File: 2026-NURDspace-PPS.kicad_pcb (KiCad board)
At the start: 4 copper layers, 50 x 50 mm, 4 parts

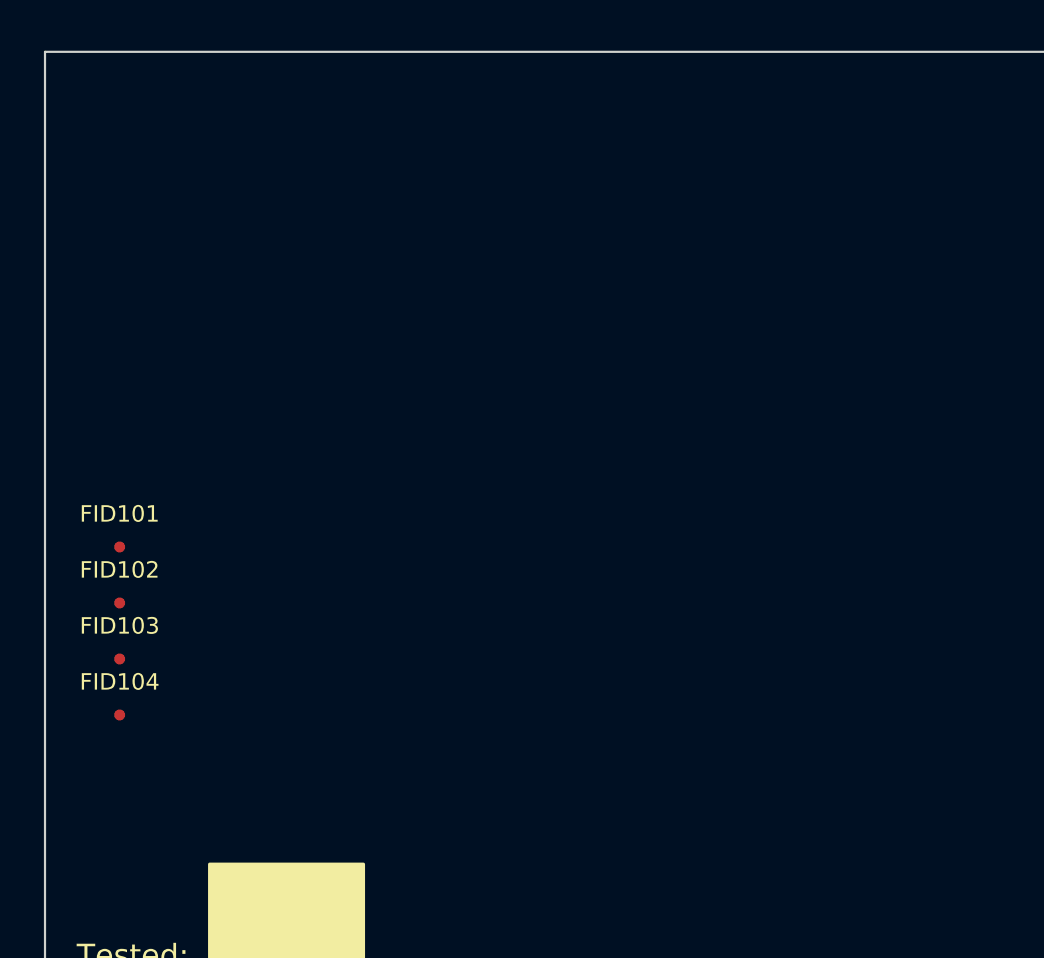
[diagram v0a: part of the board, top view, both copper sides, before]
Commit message: Started on gathering parts
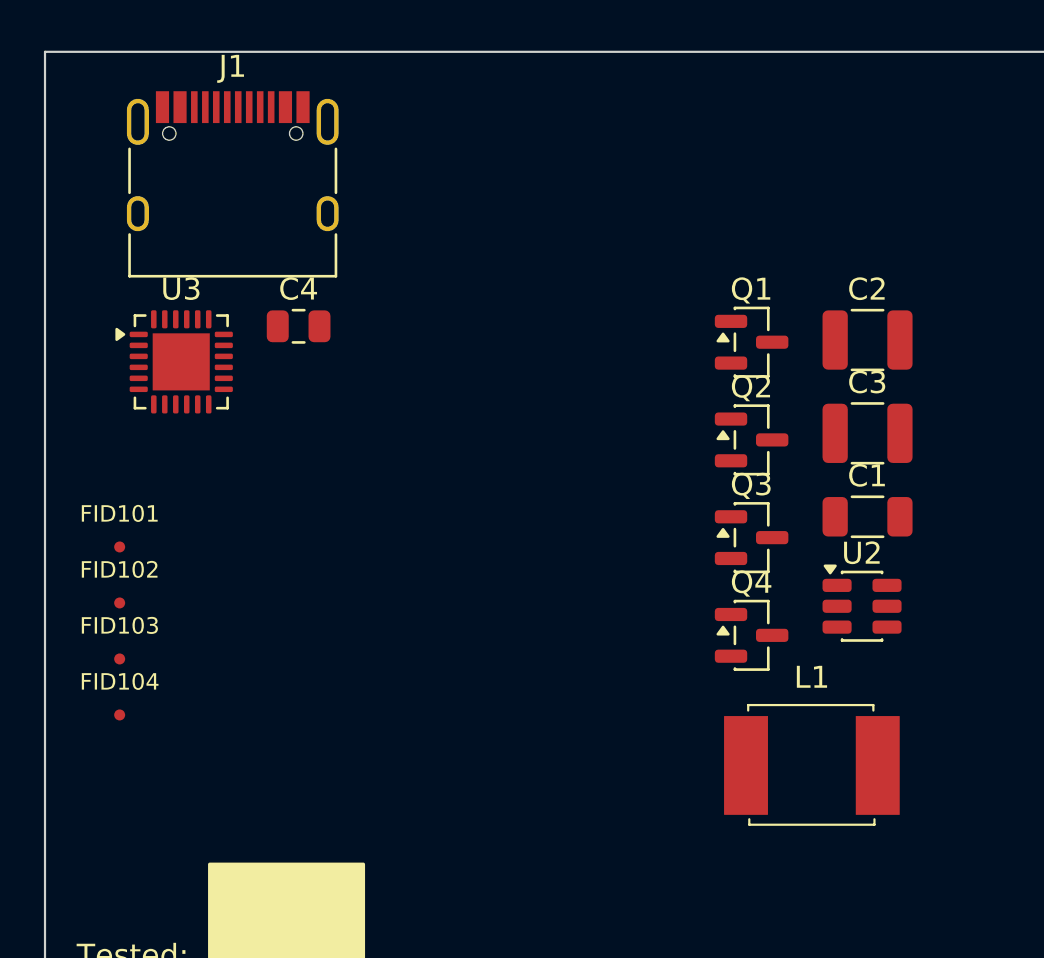
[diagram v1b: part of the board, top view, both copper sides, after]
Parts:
- added C1: 6.8uF, Capacitor_SMD:C_1206_3216Metric, F.Cu at (137.5, 71.2)
- added C2: 47uF, Capacitor_SMD:C_1210_3225Metric, F.Cu at (137.5, 63.1)
- added C3: 47uF, Capacitor_SMD:C_1210_3225Metric, F.Cu at (137.5, 67.4)
- added C4: 100nF, Capacitor_SMD:C_0805_2012Metric, F.Cu at (111.5, 62.5)
- added J1: UJ20-C-H-C-4-SMT-TR, 0_NRD_footprints:USB_C_Receptacle_SSKY_UJ20-C-H-C-4-SMT-TR, F.Cu at (108.5, 56.3)
- added L1: 4.7uH, 0_NRD_footprints:FB_2020_5650Metric, F.Cu at (134.9, 82.5)
- added Q1: BSN20, Package_TO_SOT_SMD:SOT-23, F.Cu at (132.2, 63.2)
- added Q2: BSN20, Package_TO_SOT_SMD:SOT-23, F.Cu at (132.2, 67.7)
- added Q3: BSN20, Package_TO_SOT_SMD:SOT-23, F.Cu at (132.2, 72.1)
- added Q4: BSN20, Package_TO_SOT_SMD:SOT-23, F.Cu at (132.2, 76.6)
- added U2: 3.3V, Package_TO_SOT_SMD:TSOT-23-6, F.Cu at (137.2, 75.2)
- added U3: AP33772S, Package_DFN_QFN:QFN-24-1EP_4x4mm_P0.5mm_EP2.6x2.6mm, F.Cu at (106.2, 64.1)

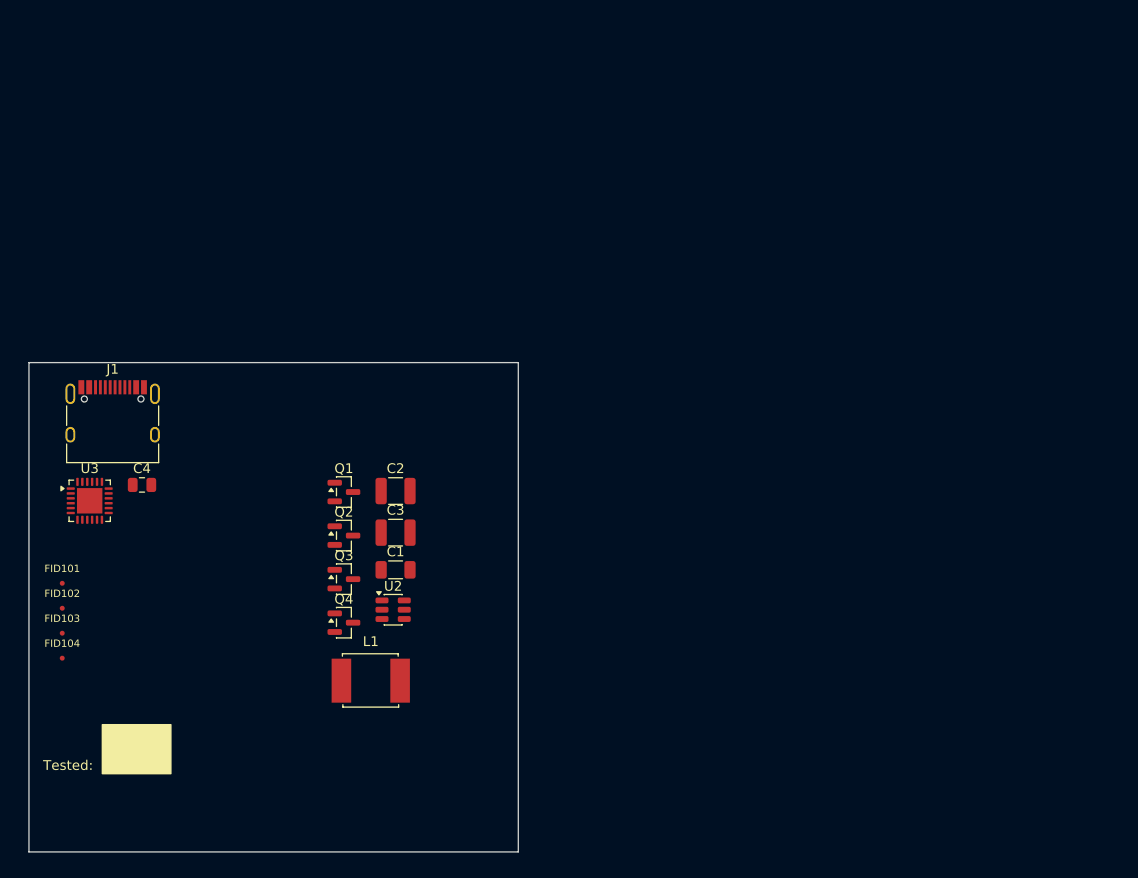
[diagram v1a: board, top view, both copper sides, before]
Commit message: Added all components
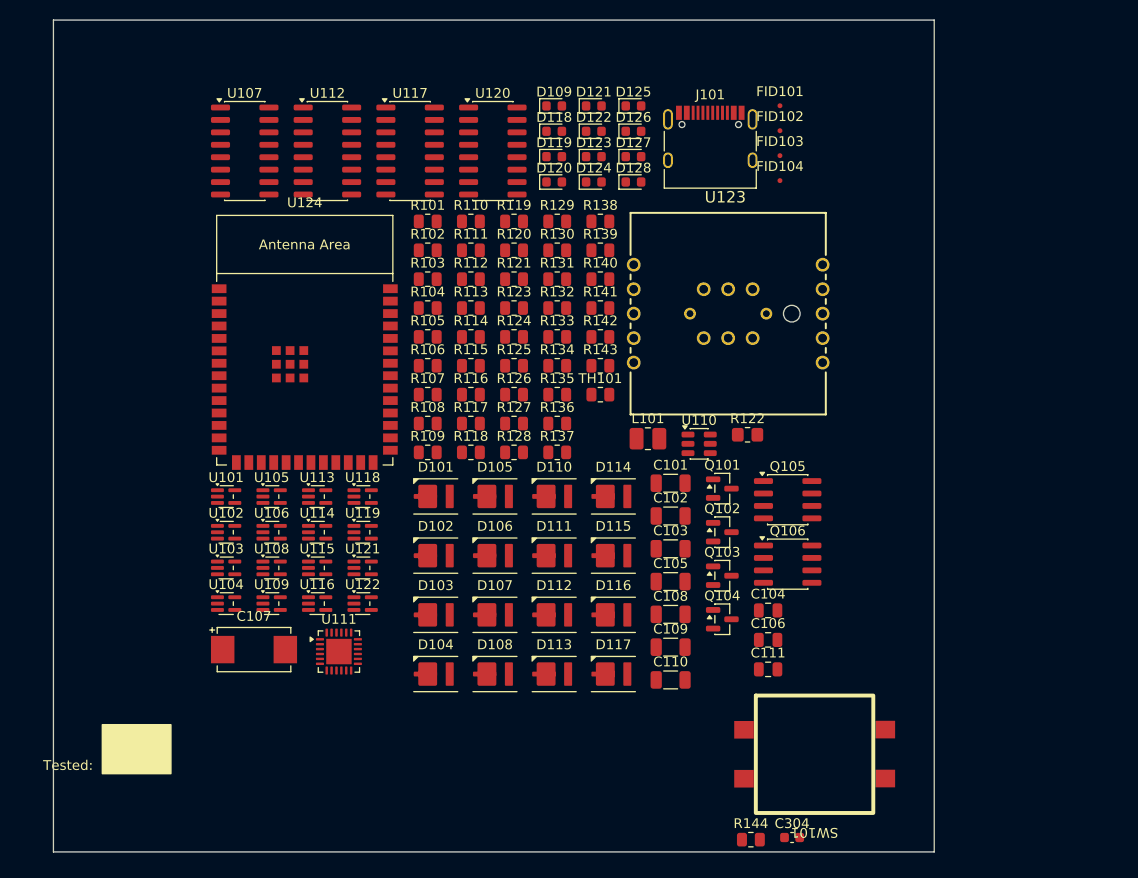
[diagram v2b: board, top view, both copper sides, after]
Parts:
- removed C1: 6.8uF, Capacitor_SMD:C_1206_3216Metric
- removed C2, C3: 47uF, Capacitor_SMD:C_1210_3225Metric
- removed C4: 100nF, Capacitor_SMD:C_0805_2012Metric
- removed J1: UJ20-C-H-C-4-SMT-TR, 0_NRD_footprints:USB_C_Receptacle_SSKY_UJ20-C-H-C-4-SMT-TR
- removed L1: 4.7uH, 0_NRD_footprints:FB_2020_5650Metric
- removed Q1, Q2, Q3, Q4: BSN20, Package_TO_SOT_SMD:SOT-23
- removed U2: 3.3V, Package_TO_SOT_SMD:TSOT-23-6
- removed U3: AP33772S, Package_DFN_QFN:QFN-24-1EP_4x4mm_P0.5mm_EP2.6x2.6mm
- added C101: 6.8uF, Capacitor_SMD:C_1206_3216Metric, F.Cu at (165.6, 62.3)
- added C102: 6.8uF, Capacitor_SMD:C_1206_3216Metric, F.Cu at (165.6, 65.7)
- added C103: 6.8uF, Capacitor_SMD:C_1206_3216Metric, F.Cu at (165.6, 69.0)
- added C104: 100nF, Capacitor_SMD:C_0805_2012Metric, F.Cu at (175.5, 75.3)
- added C105: 1uF, Capacitor_SMD:C_1206_3216Metric, F.Cu at (165.6, 72.4)
- added C106: 100nF, Capacitor_SMD:C_0805_2012Metric, F.Cu at (175.5, 78.3)
- added C107: 180uF, 0_NRD_footprints:CP_Wurth_WCAP-PHLE-L7.3W4.3H1.9, F.Cu at (123.0, 79.3)
- added C108: 6.8uF, Capacitor_SMD:C_1206_3216Metric, F.Cu at (165.6, 75.7)
- added C109: 1uF, Capacitor_SMD:C_1206_3216Metric, F.Cu at (165.6, 79.1)
- added C110: 6.8uF, Capacitor_SMD:C_1206_3216Metric, F.Cu at (165.6, 82.4)
- added C111: 100nF, Capacitor_SMD:C_0805_2012Metric, F.Cu at (175.5, 81.3)
- added C304: 100nF, Capacitor_SMD:C_0603_1608Metric, F.Cu at (178.0, 98.5)
- added D101: MXA8-PW40-0000, 0_NRD_footprints:LED_Luxeon3535_3.5x3.7mm, F.Cu at (141.6, 63.7)
- added D102: MXA8-PW40-0000, 0_NRD_footprints:LED_Luxeon3535_3.5x3.7mm, F.Cu at (141.6, 69.7)
- added D103: MXA8-PW40-0000, 0_NRD_footprints:LED_Luxeon3535_3.5x3.7mm, F.Cu at (141.6, 75.8)
- added D104: MXA8-PW40-0000, 0_NRD_footprints:LED_Luxeon3535_3.5x3.7mm, F.Cu at (141.6, 81.8)
- added D105: MXA8-PW40-0000, 0_NRD_footprints:LED_Luxeon3535_3.5x3.7mm, F.Cu at (147.6, 63.7)
- added D106: MXA8-PW40-0000, 0_NRD_footprints:LED_Luxeon3535_3.5x3.7mm, F.Cu at (147.6, 69.7)
- added D107: MXA8-PW40-0000, 0_NRD_footprints:LED_Luxeon3535_3.5x3.7mm, F.Cu at (147.6, 75.8)
- added D108: MXA8-PW40-0000, 0_NRD_footprints:LED_Luxeon3535_3.5x3.7mm, F.Cu at (147.6, 81.8)
- added D109: amber, LED_SMD:LED_0603_1608Metric, F.Cu at (153.7, 23.8)
- added D110: MXA8-PW40-0000, 0_NRD_footprints:LED_Luxeon3535_3.5x3.7mm, F.Cu at (153.7, 63.7)
- added D111: MXA8-PW40-0000, 0_NRD_footprints:LED_Luxeon3535_3.5x3.7mm, F.Cu at (153.7, 69.7)
- added D112: MXA8-PW40-0000, 0_NRD_footprints:LED_Luxeon3535_3.5x3.7mm, F.Cu at (153.7, 75.8)
- added D113: MXA8-PW40-0000, 0_NRD_footprints:LED_Luxeon3535_3.5x3.7mm, F.Cu at (153.7, 81.8)
- added D114: MXA8-PW40-0000, 0_NRD_footprints:LED_Luxeon3535_3.5x3.7mm, F.Cu at (159.7, 63.7)
- added D115: MXA8-PW40-0000, 0_NRD_footprints:LED_Luxeon3535_3.5x3.7mm, F.Cu at (159.7, 69.7)
- added D116: MXA8-PW40-0000, 0_NRD_footprints:LED_Luxeon3535_3.5x3.7mm, F.Cu at (159.7, 75.8)
- added D117: MXA8-PW40-0000, 0_NRD_footprints:LED_Luxeon3535_3.5x3.7mm, F.Cu at (159.7, 81.8)
- added D118: brightgreen, LED_SMD:LED_0603_1608Metric, F.Cu at (153.7, 26.4)
- added D119: Led_0603_superred_generic, LED_SMD:LED_0603_1608Metric, F.Cu at (153.7, 29.0)
- added D120: Led_0603_superred_generic, LED_SMD:LED_0603_1608Metric, F.Cu at (153.7, 31.5)
- added D121: Led_0603_superred_generic, LED_SMD:LED_0603_1608Metric, F.Cu at (157.7, 23.8)
- added D122: Led_0603_superred_generic, LED_SMD:LED_0603_1608Metric, F.Cu at (157.7, 26.4)
- added D123: Led_0603_superred_generic, LED_SMD:LED_0603_1608Metric, F.Cu at (157.7, 29.0)
- added D124: Led_0603_superred_generic, LED_SMD:LED_0603_1608Metric, F.Cu at (157.7, 31.5)
- added D125: Led_0603_superred_generic, LED_SMD:LED_0603_1608Metric, F.Cu at (161.8, 23.8)
- added D126: Led_0603_superred_generic, LED_SMD:LED_0603_1608Metric, F.Cu at (161.8, 26.4)
- added D127: Led_0603_superred_generic, LED_SMD:LED_0603_1608Metric, F.Cu at (161.8, 29.0)
- added D128: Led_0603_superred_generic, LED_SMD:LED_0603_1608Metric, F.Cu at (161.8, 31.5)
- added J101: UJ20-C-H-C-4-SMT-TR, 0_NRD_footprints:USB_C_Receptacle_SSKY_UJ20-C-H-C-4-SMT-TR, F.Cu at (169.6, 28.3)
- added L101: 4.7uH, Inductor_SMD:L_1008_2520Metric_Pad1.43x2.20mm_HandSolder, F.Cu at (163.2, 57.8)
- added Q101: BSN20, Package_TO_SOT_SMD:SOT-23, F.Cu at (170.8, 62.9)
- added Q102: BSN20, Package_TO_SOT_SMD:SOT-23, F.Cu at (170.8, 67.3)
- added Q103: BSN20, Package_TO_SOT_SMD:SOT-23, F.Cu at (170.8, 71.8)
- added Q104: BSN20, Package_TO_SOT_SMD:SOT-23, F.Cu at (170.8, 76.2)
- added Q105: XTR_NFET_SI4134, Package_SO:SOIC-8_3.9x4.9mm_P1.27mm, F.Cu at (177.5, 64.0)
- added Q106: XTR_NFET_SI4134, Package_SO:SOIC-8_3.9x4.9mm_P1.27mm, F.Cu at (177.5, 70.6)
- added R101: 5K1, Resistor_SMD:R_0805_2012Metric, F.Cu at (140.7, 35.6)
- added R102: 5K1, Resistor_SMD:R_0805_2012Metric, F.Cu at (140.7, 38.5)
- added R103: 5K1, Resistor_SMD:R_0805_2012Metric, F.Cu at (140.7, 41.5)
- added R104: 5K1, Resistor_SMD:R_0805_2012Metric, F.Cu at (140.7, 44.4)
- added R105: 39R, Resistor_SMD:R_0805_2012Metric, F.Cu at (140.7, 47.4)
- added R106: 39R, Resistor_SMD:R_0805_2012Metric, F.Cu at (140.7, 50.3)
- added R107: 39R, Resistor_SMD:R_0805_2012Metric, F.Cu at (140.7, 53.3)
- added R108: 39R, Resistor_SMD:R_0805_2012Metric, F.Cu at (140.7, 56.2)
- added R109: 39R, Resistor_SMD:R_0805_2012Metric, F.Cu at (140.7, 59.2)
- added R110: 39R, Resistor_SMD:R_0805_2012Metric, F.Cu at (145.2, 35.6)
- added R111: 39R, Resistor_SMD:R_0805_2012Metric, F.Cu at (145.2, 38.5)
- added R112: 39R, Resistor_SMD:R_0805_2012Metric, F.Cu at (145.2, 41.5)
- added R113: 5K1, Resistor_SMD:R_0805_2012Metric, F.Cu at (145.2, 44.4)
- added R114: 5K1, Resistor_SMD:R_0805_2012Metric, F.Cu at (145.2, 47.4)
- added R115: 5K1, Resistor_SMD:R_0805_2012Metric, F.Cu at (145.2, 50.3)
- added R116: 5K1, Resistor_SMD:R_0805_2012Metric, F.Cu at (145.2, 53.3)
- added R117: 39R, Resistor_SMD:R_0805_2012Metric, F.Cu at (145.2, 56.2)
- added R118: 39R, Resistor_SMD:R_0805_2012Metric, F.Cu at (145.2, 59.2)
- added R119: 39R, Resistor_SMD:R_0805_2012Metric, F.Cu at (149.6, 35.6)
- added R120: 39R, Resistor_SMD:R_0805_2012Metric, F.Cu at (149.6, 38.5)
- added R121: 5K1, Resistor_SMD:R_0805_2012Metric, F.Cu at (149.6, 41.5)
- added R122: 5mR, Resistor_SMD:R_0805_2012Metric_Pad1.20x1.40mm_HandSolder, F.Cu at (173.4, 57.4)
- added R123: 39R, Resistor_SMD:R_0805_2012Metric, F.Cu at (149.6, 44.4)
- added R124: 39R, Resistor_SMD:R_0805_2012Metric, F.Cu at (149.6, 47.4)
- added R125: 39R, Resistor_SMD:R_0805_2012Metric, F.Cu at (149.6, 50.3)
- added R126: 39R, Resistor_SMD:R_0805_2012Metric, F.Cu at (149.6, 53.3)
- added R127: 5K1, Resistor_SMD:R_0805_2012Metric, F.Cu at (149.6, 56.2)
- added R128: 5K1, Resistor_SMD:R_0805_2012Metric, F.Cu at (149.6, 59.2)
- added R129: 180R, Resistor_SMD:R_0805_2012Metric, F.Cu at (154.0, 35.6)
- added R130: 5K1, Resistor_SMD:R_0805_2012Metric, F.Cu at (154.0, 38.5)
- added R131: 5K1, Resistor_SMD:R_0805_2012Metric, F.Cu at (154.0, 41.5)
- added R132: 270R, Resistor_SMD:R_0805_2012Metric, F.Cu at (154.0, 44.4)
- added R133: 270R, Resistor_SMD:R_0805_2012Metric, F.Cu at (154.0, 47.4)
- added R134: 270R, Resistor_SMD:R_0805_2012Metric, F.Cu at (154.0, 50.3)
- added R135: 270R, Resistor_SMD:R_0805_2012Metric, F.Cu at (154.0, 53.3)
- added R136: 270R, Resistor_SMD:R_0805_2012Metric, F.Cu at (154.0, 56.2)
- added R137: 5K1, Resistor_SMD:R_0805_2012Metric, F.Cu at (154.0, 59.2)
- added R138: 5K1, Resistor_SMD:R_0805_2012Metric, F.Cu at (158.4, 35.6)
- added R139: 270R, Resistor_SMD:R_0805_2012Metric, F.Cu at (158.4, 38.5)
- added R140: 270R, Resistor_SMD:R_0805_2012Metric, F.Cu at (158.4, 41.5)
- added R141: 270R, Resistor_SMD:R_0805_2012Metric, F.Cu at (158.4, 44.4)
- added R142: 270R, Resistor_SMD:R_0805_2012Metric, F.Cu at (158.4, 47.4)
- added R143: 270R, Resistor_SMD:R_0805_2012Metric, F.Cu at (158.4, 50.3)
- added R144: 5K1, Resistor_SMD:R_0805_2012Metric, F.Cu at (173.8, 98.7)
- added SW101: 430172085816, 0_NRD_footprints:btn_momentary_430172085816, F.Cu at (180.3, 90.0)
- added TH101: NTCS0805, Resistor_SMD:R_0805_2012Metric, F.Cu at (158.4, 53.3)
- added U101: 1G126, Package_TO_SOT_SMD:SOT-353_SC-70-5, F.Cu at (120.1, 63.7)
- added U102: 1G126, Package_TO_SOT_SMD:SOT-353_SC-70-5, F.Cu at (120.1, 67.3)
- added U103: 1G126, Package_TO_SOT_SMD:SOT-353_SC-70-5, F.Cu at (120.1, 71.0)
- added U104: 1G126, Package_TO_SOT_SMD:SOT-353_SC-70-5, F.Cu at (120.1, 74.6)
- added U105: 1G126, Package_TO_SOT_SMD:SOT-353_SC-70-5, F.Cu at (124.8, 63.7)
- added U106: 1G126, Package_TO_SOT_SMD:SOT-353_SC-70-5, F.Cu at (124.8, 67.3)
- added U107: 74HC595, Package_SO:SOIC-16_3.9x9.9mm_P1.27mm, F.Cu at (122.0, 28.4)
- added U108: 1G126, Package_TO_SOT_SMD:SOT-353_SC-70-5, F.Cu at (124.8, 71.0)
- added U109: 1G126, Package_TO_SOT_SMD:SOT-353_SC-70-5, F.Cu at (124.8, 74.6)
- added U110: 3.3V, Package_TO_SOT_SMD:TSOT-23-6, F.Cu at (168.5, 58.3)
- added U111: AP33772S, Package_DFN_QFN:QFN-24-1EP_4x4mm_P0.5mm_EP2.6x2.6mm, F.Cu at (131.7, 79.5)
- added U112: 74HC595, Package_SO:SOIC-16_3.9x9.9mm_P1.27mm, F.Cu at (130.5, 28.4)
- added U113: 1G126, Package_TO_SOT_SMD:SOT-353_SC-70-5, F.Cu at (129.4, 63.7)
- added U114: 1G126, Package_TO_SOT_SMD:SOT-353_SC-70-5, F.Cu at (129.4, 67.3)
- added U115: 1G126, Package_TO_SOT_SMD:SOT-353_SC-70-5, F.Cu at (129.4, 71.0)
- added U116: 1G126, Package_TO_SOT_SMD:SOT-353_SC-70-5, F.Cu at (129.4, 74.6)
- added U117: 74HC595, Package_SO:SOIC-16_3.9x9.9mm_P1.27mm, F.Cu at (138.9, 28.4)
- added U118: 1G126, Package_TO_SOT_SMD:SOT-353_SC-70-5, F.Cu at (134.1, 63.7)
- added U119: 1G126, Package_TO_SOT_SMD:SOT-353_SC-70-5, F.Cu at (134.1, 67.3)
- added U120: 74HC595, Package_SO:SOIC-16_3.9x9.9mm_P1.27mm, F.Cu at (147.4, 28.4)
- added U121: 1G126, Package_TO_SOT_SMD:SOT-353_SC-70-5, F.Cu at (134.1, 71.0)
- added U122: 1G126, Package_TO_SOT_SMD:SOT-353_SC-70-5, F.Cu at (134.1, 74.6)
- added U123: 481RV12172100, 0_NRD_footprints:481RV12172100, F.Cu at (171.4, 45.0)
- added U124: ESP32-S3-WROOM-1, 0_NRD_footprints:ESP32-S3-WROOM-1, F.Cu at (128.2, 50.7)
- moved FID101 88.1 mm to (176.7, 23.8)
- moved FID102 88.1 mm to (176.7, 26.3)
- moved FID103 88.1 mm to (176.7, 28.9)
- moved FID104 88.1 mm to (176.7, 31.4)
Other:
- board size 50 x 50 mm -> 90 x 85 mm
